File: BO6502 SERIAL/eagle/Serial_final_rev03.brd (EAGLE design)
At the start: 101.6 x 65 mm, 18 parts, among them IC1 MAX232, IC2 74AC138N, Q1 1.8432MHz, U1 65C51, X1 RS232-DB9

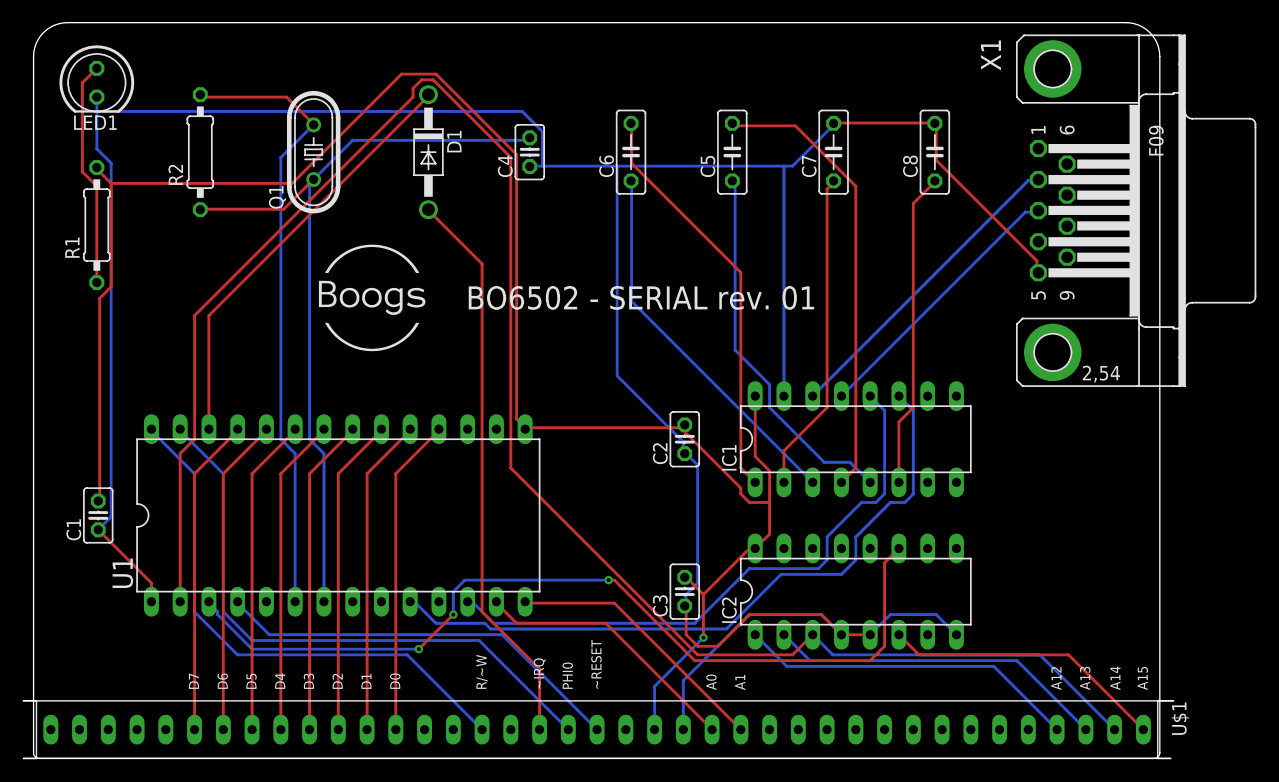
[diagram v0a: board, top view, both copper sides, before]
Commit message: add SERIAL PCB
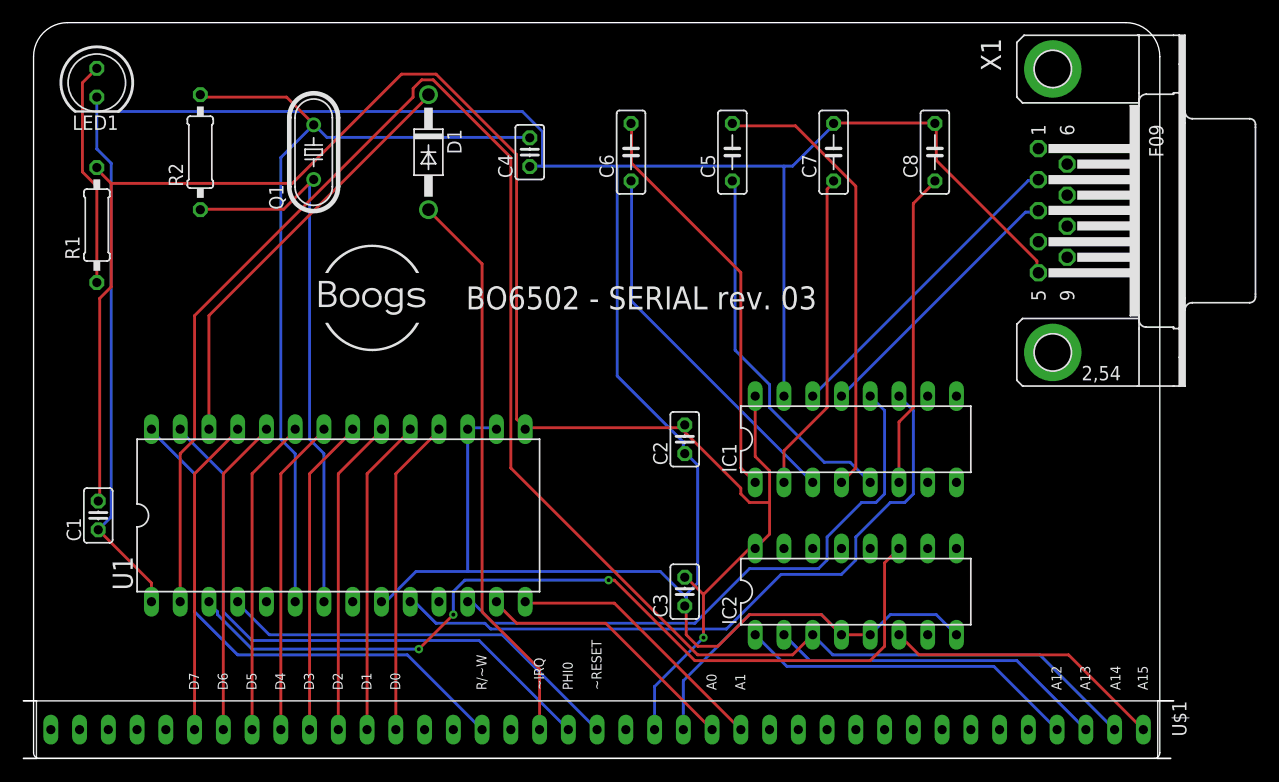
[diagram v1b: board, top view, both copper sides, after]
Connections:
- net GND: now also U1.16, U1.17, U1.9
- net N$11: now also C4.2
- net N$12: no longer C4.2
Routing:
- net GND: track 259.7 -> 304.1 mm
- net N$12: track 69.8 -> 49.3 mm
- net N$11: track 55.1 -> 74.7 mm
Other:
- board text added: "BO6502 - SERIAL rev. 03"
- board text removed: "BO6502 - SERIAL rev. 01"
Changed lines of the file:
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@@
 <?xml version="1.0" encoding="utf-8"?>
 <!DOCTYPE eagle SYSTEM "eagle.dtd">
-<eagle version="9.6.0">
+<eagle version="9.6.2">
 <drawing>
 <settings>
@@
 <wire x1="99.314" y1="5.08" x2="100.711" y2="5.08" width="0.1524" layer="20"/>
 <wire x1="99.314" y1="0" x2="100.457" y2="0" width="0.1524" layer="20"/>
-<text x="38.2016" y="39.6654" size="2.032" layer="25" rot="SR0">BO6502 - SERIAL rev. 01</text>
-<text x="70.7136" y="39.6654" size="2.032" layer="26" rot="SMR0">BO6502 - SERIAL rev. 01</text>
+<text x="38.2016" y="39.6654" size="2.032" layer="25" rot="SR0">BO6502 - SERIAL rev. 03</text>
+<text x="70.7136" y="39.6654" size="2.032" layer="26" rot="SMR0">BO6502 - SERIAL rev. 03</text>
 <rectangle x1="29.85008125" y1="35.971478125" x2="29.972" y2="35.981634375" layer="25"/>
 <rectangle x1="29.585921875" y1="35.9816375" x2="30.236159375" y2="35.99179375" layer="25"/>
@@
 <attribute name="VALUE" x="6.223" y="44.8564" size="1.27" layer="27" ratio="10" rot="R90"/>
 </element>
-<element name="LED1" library="led" library_urn="urn:adsk.eagle:library:259" package="LED5MM" package3d_urn="urn:adsk.eagle:package:15799/2" value="RED" x="5.588" y="59.69" smashed="yes" rot="R270">
+<element name="LED1" library="led" library_urn="urn:adsk.eagle:library:259" package="LED5MM" package3d_urn="urn:adsk.eagle:package:15799/2" override_package3d_urn="urn:adsk.eagle:package:51395390/2" override_package_urn="urn:adsk.eagle:footprint:15655/1" value="RED" x="5.588" y="59.69" smashed="yes" rot="R270">
 <attribute name="NAME" x="3.429" y="55.5244" size="1.27" layer="25" ratio="10"/>
 <attribute name="POPULARITY" value="93" x="7.747" y="59.69" size="1.778" layer="27" rot="R270" display="off"/>
@@
 <attribute name="VALUE" x="17.145" y="20.574" size="1.778" layer="27"/>
 </element>
-<element name="D1" library="diode" library_urn="urn:adsk.eagle:library:210" package="DO41-10" package3d_urn="urn:adsk.eagle:package:43336/1" value="BS140" x="34.88870625" y="53.5559" smashed="yes" rot="R270">
+<element name="D1" library="diode" library_urn="urn:adsk.eagle:library:210" package="DO41-10" package3d_urn="urn:adsk.eagle:package:43336/1" override_package3d_urn="urn:adsk.eagle:package:51395389/2" override_package_urn="urn:adsk.eagle:footprint:43094/1" value="BS140" x="34.88870625" y="53.5559" smashed="yes" rot="R270">
 <attribute name="NAME" x="36.53970625" y="55.5879" size="1.27" layer="25" ratio="10" rot="R270"/>
 <attribute name="POPULARITY" value="82" x="34.88870625" y="53.5559" size="1.778" layer="27" rot="R270" display="off"/>
@@
 <wire x1="6.858" y1="21.336" x2="6.858" y2="52.578" width="0.254" layer="16"/>
 <wire x1="5.715" y1="20.193" x2="6.858" y2="21.336" width="0.254" layer="16"/>
-<wire x1="57.658" y1="14.478" x2="57.658" y2="13.462" width="0.254" layer="16"/>
+<wire x1="57.658" y1="14.478" x2="57.658" y2="14.224" width="0.254" layer="16"/>
+<wire x1="57.658" y1="14.224" x2="57.658" y2="13.462" width="0.254" layer="16"/>
 <wire x1="58.674" y1="15.494" x2="57.658" y2="14.478" width="0.254" layer="16"/>
 <wire x1="58.674" y1="25.908" x2="58.674" y2="15.494" width="0.254" layer="16"/>
@@
 <wire x1="44.958" y1="55.372" x2="43.18" y2="57.15" width="0.254" layer="16"/>
 <wire x1="44.958" y1="52.324" x2="44.958" y2="55.372" width="0.254" layer="16"/>
+<contactref element="U1" pad="9"/>
+<wire x1="31.242" y1="13.97" x2="30.734" y2="13.97" width="0.254" layer="16"/>
+<wire x1="33.782" y1="16.51" x2="31.242" y2="13.97" width="0.254" layer="16"/>
+<wire x1="55.372" y1="16.51" x2="38.354" y2="16.51" width="0.254" layer="16"/>
+<wire x1="38.354" y1="16.51" x2="33.782" y2="16.51" width="0.254" layer="16"/>
+<wire x1="57.658" y1="14.224" x2="55.372" y2="16.51" width="0.254" layer="16"/>
+<wire x1="30.734" y1="13.97" x2="30.734" y2="13.843" width="0.254" layer="16"/>
+<contactref element="U1" pad="17"/>
+<contactref element="U1" pad="16"/>
+<wire x1="40.894" y1="29.21" x2="38.354" y2="29.21" width="0.254" layer="16"/>
+<wire x1="38.354" y1="29.21" x2="38.354" y2="29.083" width="0.254" layer="16"/>
+<wire x1="40.894" y1="29.21" x2="40.894" y2="29.083" width="0.254" layer="16"/>
+<wire x1="38.354" y1="16.51" x2="38.354" y2="29.083" width="0.254" layer="16"/>
 </signal>
 <signal name="VCC">
@@
 <wire x1="24.638" y1="55.88" x2="21.844" y2="53.086" width="0.254" layer="16"/>
 <wire x1="24.638" y1="55.88" x2="24.746853125" y2="55.9689" width="0.254" layer="16"/>
+<contactref element="C4" pad="2"/>
+<wire x1="25.908" y1="54.864" x2="43.688" y2="54.864" width="0.254" layer="16"/>
+<wire x1="24.892" y1="55.88" x2="25.908" y2="54.864" width="0.254" layer="16"/>
+<wire x1="43.688" y1="54.864" x2="43.836759375" y2="54.8259" width="0.254" layer="16"/>
+<wire x1="24.892" y1="55.88" x2="24.746853125" y2="55.9689" width="0.254" layer="16"/>
 </signal>
 <signal name="N$12">
@@
 <contactref element="R2" pad="1"/>
 <contactref element="U1" pad="7"/>
-<contactref element="C4" pad="2"/>
 <wire x1="22.098" y1="48.514" x2="14.732" y2="48.514" width="0.254" layer="1"/>
 <wire x1="24.638" y1="51.054" x2="22.098" y2="48.514" width="0.254" layer="1"/>
@@
 <wire x1="24.638" y1="51.054" x2="24.384" y2="50.8" width="0.254" layer="16"/>
 <wire x1="24.638" y1="51.054" x2="24.746853125" y2="51.1429" width="0.254" layer="16"/>
-<wire x1="28.194" y1="54.61" x2="43.688" y2="54.61" width="0.254" layer="16"/>
-<wire x1="24.892" y1="51.308" x2="28.194" y2="54.61" width="0.254" layer="16"/>
-<wire x1="43.688" y1="54.61" x2="43.836759375" y2="54.8259" width="0.254" layer="16"/>
 <wire x1="24.892" y1="51.308" x2="24.746853125" y2="51.1429" width="0.254" layer="16"/>
 </signal>
@@
 </signals>
 <mfgpreviewcolors>
-<mfgpreviewcolor name="soldermaskcolor" color="0xC8008000"/>
+<mfgpreviewcolor name="soldermaskcolor" color="0xC859007F"/>
 <mfgpreviewcolor name="silkscreencolor" color="0xFFFEFEFE"/>
 <mfgpreviewcolor name="backgroundcolor" color="0xFF282828"/>
@@
 packages will not be understood (or retained) with this version.
 </note>
+<note version="9.4" severity="warning">
+Since Version 9.4, EAGLE supports the overriding of 3D packages
+in schematics and board files. Those overridden 3d packages
+will not be understood (or retained) with this version.
+</note>
 </compatibility>
